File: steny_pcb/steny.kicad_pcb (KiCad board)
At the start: 2 copper layers, 0 parts

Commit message: Finished PCB
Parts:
- added A1: RaspberryPi_Pico, Module:RaspberryPi_Pico_Common_Unspecified, F.Cu at (141.8, 88.5)
- added CP1: Copper Pad 14.5x16.5, customs:copper_pad_14_5x16_5, F.Cu at (54.7, 71.5)
- added CP10: Copper Pad 14.5x16.5, customs:copper_pad_14_5x16_5, F.Cu at (229.0, 93.2)
- added CP11: Copper Pad 14.5x16.5, customs:copper_pad_14_5x16_5, F.Cu at (248.2, 93.2)
- added CP12: Copper Pad 14.5x16.5, customs:copper_pad_14_5x16_5, F.Cu at (54.7, 93.2)
- added CP13: Copper Pad 14.5x16.5, customs:copper_pad_14_5x16_5, F.Cu at (73.9, 93.2)
- added CP14: Copper Pad 14.5x16.5, customs:copper_pad_14_5x16_5, F.Cu at (93.2, 93.2)
- added CP15: Copper Pad 14.5x16.5, customs:copper_pad_14_5x16_5, F.Cu at (103.4, 135.1)
- added CP16: Copper Pad 14.5x16.5, customs:copper_pad_14_5x16_5, F.Cu at (160.9, 135.1)
- added CP17: Copper Pad 14.5x16.5, customs:copper_pad_14_5x16_5, F.Cu at (199.2, 135.1)
- added CP18: Copper Pad 14.5x16.5, customs:copper_pad_14_5x16_5, F.Cu at (190.5, 93.2)
- added CP19: Copper Pad 14.5x16.5, customs:copper_pad_14_5x16_5, F.Cu at (267.5, 93.2)
- added CP2: Copper Pad 14.5x16.5, customs:copper_pad_14_5x16_5, F.Cu at (73.9, 71.5)
- added CP20: Copper Pad 14.5x16.5, customs:copper_pad_14_5x16_5, F.Cu at (229.0, 71.5)
- added CP21: Copper Pad 14.5x16.5, customs:copper_pad_14_5x16_5, F.Cu at (248.2, 71.5)
- added CP22: Copper Pad 14.5x16.5, customs:copper_pad_14_5x16_5, F.Cu at (267.5, 71.5)
- added CP23: Copper Pad 14.5x38, customs:copper_pad_14_5x38, F.Cu at (171.2, 82.5)
- added CP24: Copper Pad 14.5x38, customs:copper_pad_14_5x38, F.Cu at (112.4, 82.5)
- added CP25: Copper Pad 14.5x38, customs:copper_pad_14_5x38, F.Cu at (35.5, 82.5)
- added CP3: Copper Pad 14.5x16.5, customs:copper_pad_14_5x16_5, F.Cu at (93.2, 71.5)
- added CP4: Copper Pad 14.5x16.5, customs:copper_pad_14_5x16_5, F.Cu at (84.2, 135.1)
- added CP5: Copper Pad 14.5x16.5, customs:copper_pad_14_5x16_5, F.Cu at (122.7, 135.1)
- added CP6: Copper Pad 14.5x16.5, customs:copper_pad_14_5x16_5, F.Cu at (180.2, 135.1)
- added CP7: Copper Pad 14.5x16.5, customs:copper_pad_14_5x16_5, F.Cu at (190.5, 71.5)
- added CP8: Copper Pad 14.5x16.5, customs:copper_pad_14_5x16_5, F.Cu at (209.8, 71.5)
- added CP9: Copper Pad 14.5x16.5, customs:copper_pad_14_5x16_5, F.Cu at (209.8, 93.2)
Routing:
- net Net-(A1-GPIO22): track 0.00 -> 157.5 mm, vias 0 -> 1
- net Net-(A1-GPIO20): track 0.00 -> 139.2 mm, vias 0 -> 1
- net Net-(A1-GPIO21): track 0.00 -> 133.4 mm, vias 0 -> 1
- net Net-(A1-GPIO18): track 0.00 -> 120.8 mm, vias 0 -> 1
- net Net-(A1-GPIO5): track 0.00 -> 116.1 mm, vias 0 -> 1
- net Net-(A1-GPIO19): track 0.00 -> 114.7 mm, vias 0 -> 1
- net Net-(A1-GPIO16): track 0.00 -> 105.8 mm, vias 0 -> 1
- net Net-(A1-GPIO0): track 0.00 -> 105.0 mm, vias 0 -> 1
- net Net-(A1-GPIO12): track 0.00 -> 103.5 mm, vias 0 -> 1
- net Net-(A1-GPIO15): track 0.00 -> 103.0 mm, vias 0 -> 1
- net Net-(A1-GPIO17): track 0.00 -> 98.0 mm, vias 0 -> 1
- net Net-(A1-GPIO2): track 0.00 -> 94.7 mm, vias 0 -> 1
- net Net-(A1-GPIO11): track 0.00 -> 92.0 mm, vias 0 -> 1
- net Net-(A1-GPIO10): track 0.00 -> 81.8 mm, vias 0 -> 1
- net Net-(A1-GPIO7): track 0.00 -> 80.9 mm, vias 0 -> 1
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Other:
- board outline added: 249.5 x 83.2 mm

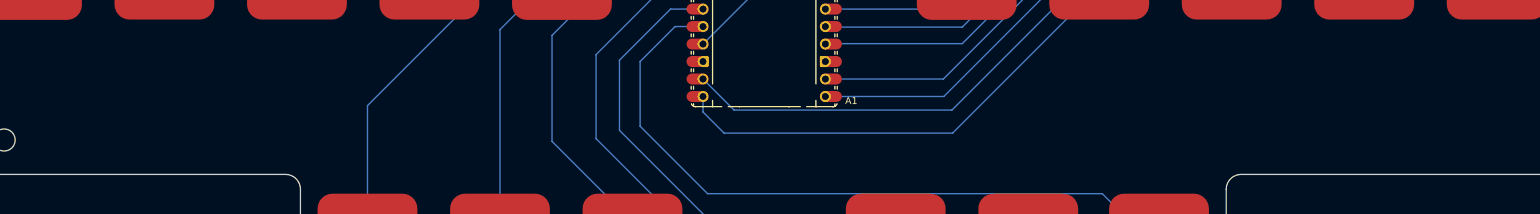
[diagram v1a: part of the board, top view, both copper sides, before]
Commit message: added text to the pcb
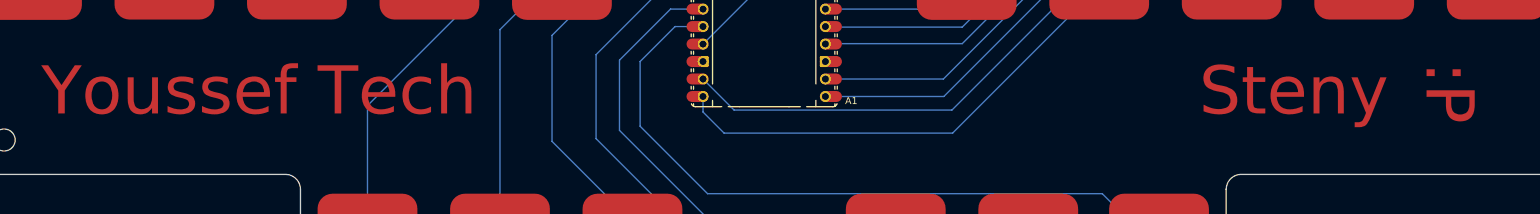
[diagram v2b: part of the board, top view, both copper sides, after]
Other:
- board text added: ":P"
- board text added: "Steny"
- board text added: "Youssef Tech"
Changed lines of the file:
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@@
 		(layer "Edge.Cuts")
+	)
+	(gr_text "Youssef Tech"
+		(at 36.8 116 0)
+		(layer "F.Cu")
+		(effects
+			(font
+				(size 7 7)
+				(thickness 1)
+			)
+			(justify left bottom)
+		)
+	)
+	(gr_text "Steny"
+		(at 205 116 0)
+		(layer "F.Cu")
+		(effects
+			(font
+				(size 7 7)
+				(thickness 1)
+			)
+			(justify left bottom)
+		)
+	)
+	(gr_text ":P"
+		(at 237.2 107.6 270)
+		(layer "F.Cu")
+		(effects
+			(font
+				(size 7 7)
+				(thickness 1)
+			)
+			(justify left bottom)
+		)
+	)
+	(gr_text ":P"
+		(at 237.2 107.6 270)
+		(layer "F.Mask")
+		(effects
+			(font
+				(size 7 7)
+				(thickness 1)
+			)
+			(justify left bottom)
+		)
+	)
+	(gr_text "Youssef Tech"
+		(at 36.8 116 0)
+		(layer "F.Mask")
+		(effects
+			(font
+				(size 7 7)
+				(thickness 1)
+			)
+			(justify left bottom)
+		)
+	)
+	(gr_text "Steny"
+		(at 205 116 0)
+		(layer "F.Mask")
+		(effects
+			(font
+				(size 7 7)
+				(thickness 1)
+			)
+			(justify left bottom)
+		)
 	)
 	(via
